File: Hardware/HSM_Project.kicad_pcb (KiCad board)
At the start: 2 copper layers, 139 x 101.5 mm, 116 parts, among them J1 Conn_01x02_Pin, J10 VL530X Connector, J11 VL530X Connector, J12 VL530X Connector, J13 VL530X Connector, J14 Conn_01x04_Pin, J15 BNO055 Breakout, J16 HC-05 Breakout Board, J17 Conn_01x04_Pin, J18 Conn_01x02_Pin, J19 Conn_01x02_Pin, J2 MP1584 Breakout, J20 Conn_01x04_Pin, J3 DRV8833 Breakout, J4 TEENSY_4.1, J8 VL530X Connector, J9 VL530X Connector, Q1 Q_NMOS_GSD, Q10 Q_NMOS_GSD, Q11 Q_NMOS_GSD, Q12 Q_NMOS_GSD, Q13 TEFT4300, Q2 Q_NMOS_GSD, Q3 TEFT4300, Q4 TEFT4300, Q5 TEFT4300, Q6 TEFT4300, Q7 TEFT4300, Q8 Q_NMOS_GSD, Q9 Q_NMOS_GSD, SW1 SW_SPDT, SW2 SW_SPDT, SW3 SW_Push, SW4 SW_Push

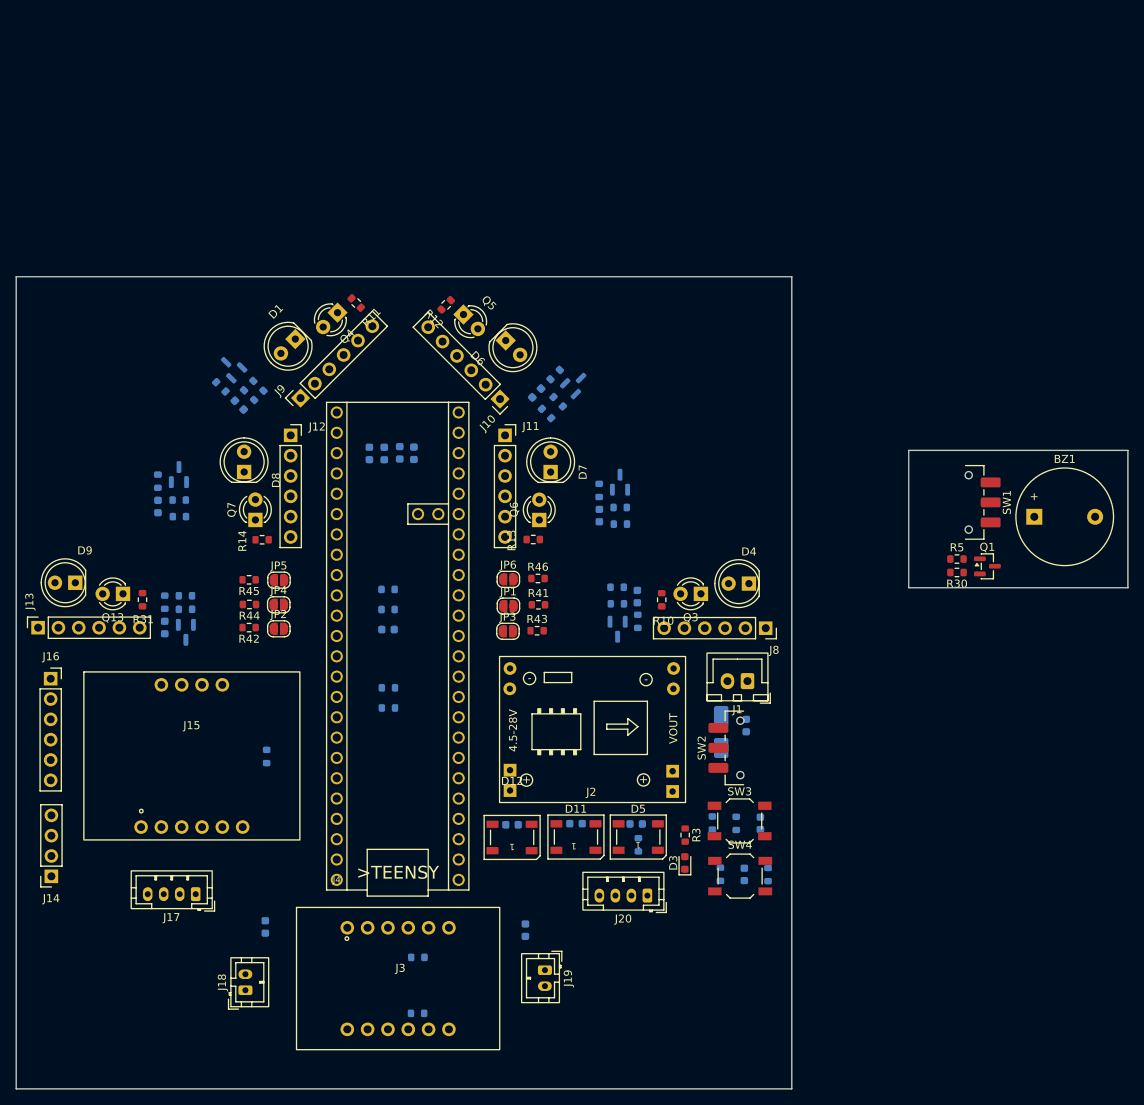
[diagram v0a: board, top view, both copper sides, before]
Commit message: Added the mounting holes, kill iwtch for the moto,removed resistors from xshut, and some others
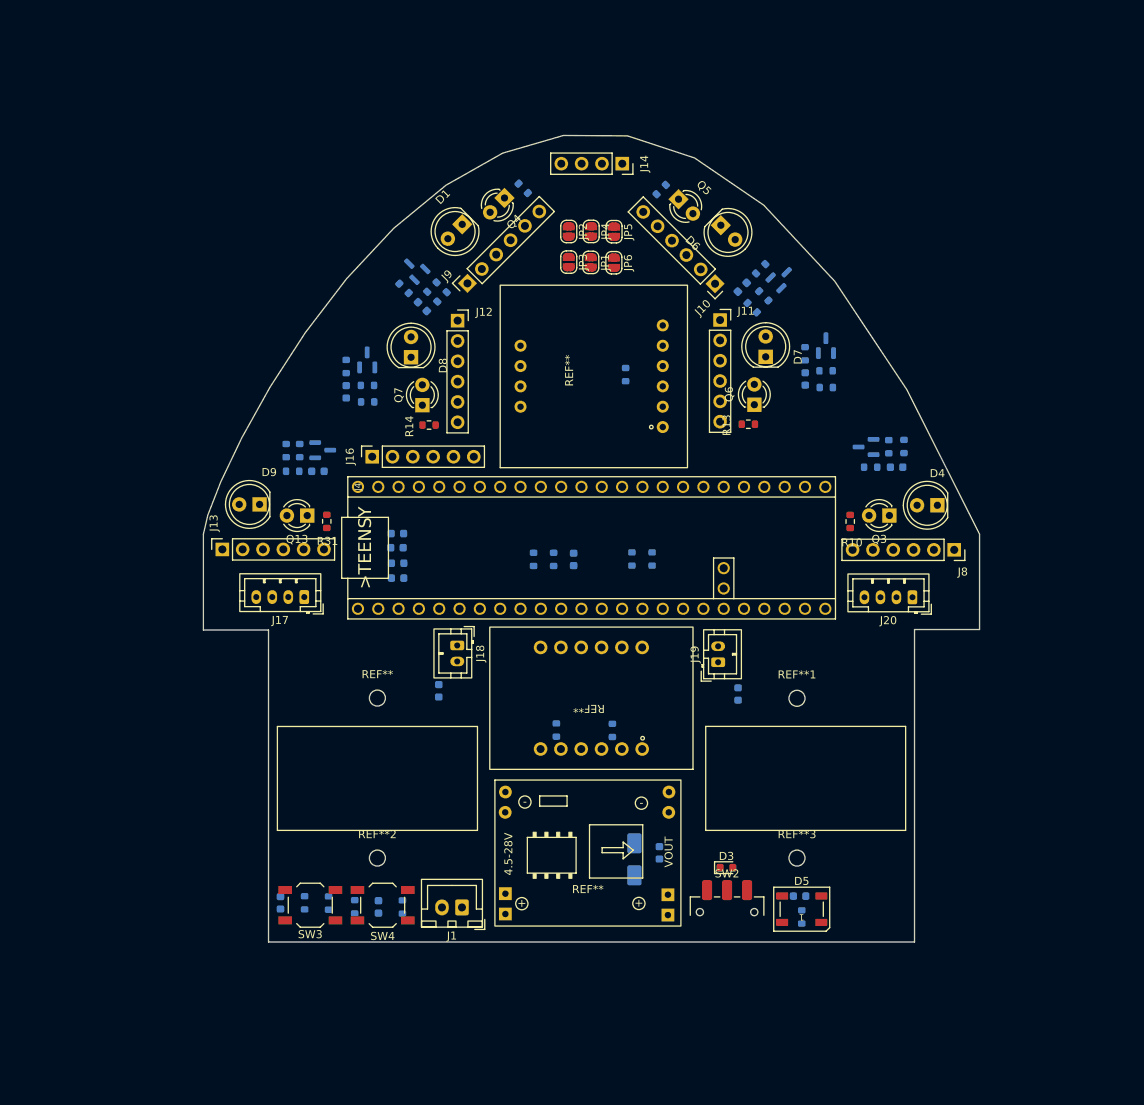
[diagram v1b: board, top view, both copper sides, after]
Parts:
- removed BZ1: Buzzer, Buzzer_Beeper:Buzzer_12x9.5RM7.6
- removed C14, C15: 100n, Capacitor_SMD:C_0603_1608Metric
- removed D11, D12: WS2812B, LED_SMD:LED_WS2812B_PLCC4_5.0x5.0mm_P3.2mm
- removed J15: BNO055 Breakout, Micromouse_Footprints:BNO055
- removed J2: MP1584 Breakout, Micromouse_Footprints:SRT_MPT1584EN_Module
- removed J3: DRV8833 Breakout, Micromouse_Footprints:DRV8833
- removed Q1: Q_NMOS_GSD, Package_TO_SOT_SMD:SOT-23
- removed R30, R41, R42, R43, R44, R45, R46, R5: 10k, Resistor_SMD:R_0603_1608Metric
- removed SW1: SW_SPDT, Button_Switch_SMD:SW_SPDT_CK_JS102011SAQN
- added REF**: MP1584, Micromouse_Footprints:MP1584, F.Cu at (153.0, 120.9)
- added REF**: MountingHole_2mm, MountingHole:MountingHole_2mm, F.Cu at (126.8, 100.5)
- added REF**: BNO055, Micromouse_Footprints:BNO055, F.Cu at (154.0, 60.0)
- added REF**: DRV8833, Micromouse_Footprints:DRV8833, F.Cu at (153.5, 100.5)
- added REF**1: MountingHole_2mm, MountingHole:MountingHole_2mm, F.Cu at (179.2, 100.5)
- added REF**2: MountingHole_2mm, MountingHole:MountingHole_2mm, F.Cu at (126.8, 120.5)
- added REF**3: MountingHole_2mm, MountingHole:MountingHole_2mm, F.Cu at (179.2, 120.5)
- R11, R12, R3: moved to B.Cu
- moved J14 114.1 mm to (157.4, 33.7), turned to -90 degrees
- moved R47 65.5 mm to (157.8, 60.1)
- moved JP2 61.5 mm to (150.7, 42.2), turned to -90 degrees
- moved JP4 60.9 mm to (153.5, 42.2), turned to -90 degrees
- moved C17 60.8 mm to (114.7, 126.1), turned to -90 degrees
- moved JP5 60.4 mm to (156.3, 42.2), turned to -90 degrees
- moved R27 54.9 mm to (117.7, 126.1), turned to -90 degrees
- moved SW3 54.7 mm to (118.4, 126.4), turned to 0 degrees
- moved R1 51.8 mm to (123.9, 126.6), turned to -90 degrees
- moved J18 50.6 mm to (136.8, 93.9), turned to -90 degrees
- moved J20 49.9 mm to (193.7, 87.9)
- moved J4 49.2 mm to (124.3, 74.1), turned to -90 degrees
- moved R2 49.0 mm to (120.7, 126.1), turned to -90 degrees
- moved J16 48.8 mm to (126.1, 70.3), turned to 90 degrees
- moved JP3 46.8 mm to (150.7, 46.0), turned to -90 degrees
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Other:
- board size 139 x 101.5 mm -> 97 x 100.8 mm
- board text added: "${REFERENCE}"

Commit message: 1)PCB tracing continued, power traces need to verified,signal traces almost done except xshut, need to verify drv8833 dimesnions, should resolve teensy 4.1 error, switches footprint need to be changed. 2) changed schematic for optimum tracing in pcb editor,removed oled and added one more extra i2c bus to prevent i2c locking
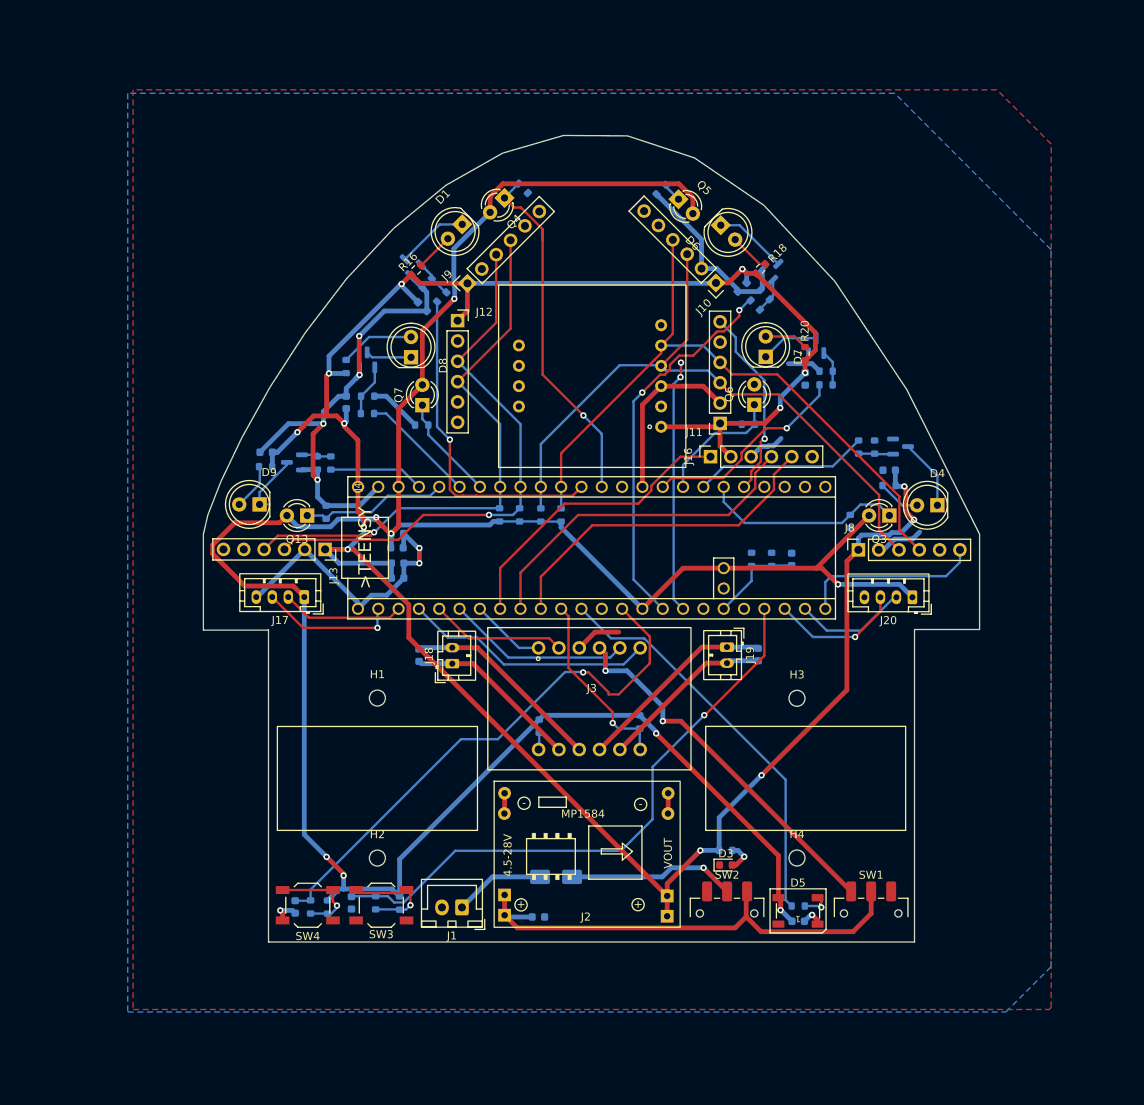
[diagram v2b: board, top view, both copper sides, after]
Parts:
- removed J14: Conn_01x04_Pin, Connector_PinSocket_2.54mm:PinSocket_1x04_P2.54mm_Vertical
- removed JP1, JP2, JP3, JP4, JP5, JP6: SolderJumper_2_Bridged, Jumper:SolderJumper-2_P1.3mm_Open_RoundedPad1.0x1.5mm
- removed R47: 10k, Resistor_SMD:R_0603_1608Metric
- removed REF**: MP1584, Micromouse_Footprints:MP1584
- removed REF**, REF**1, REF**2, REF**3: MountingHole_2mm, MountingHole:MountingHole_2mm
- removed REF**: BNO055, Micromouse_Footprints:BNO055
- removed REF**: DRV8833, Micromouse_Footprints:DRV8833
- added H1: MountingHole, MountingHole:MountingHole_2mm, F.Cu at (126.8, 100.5)
- added H2: MountingHole, MountingHole:MountingHole_2mm, F.Cu at (126.8, 120.5)
- added H3: MountingHole, MountingHole:MountingHole_2mm, F.Cu at (179.2, 100.5)
- added H4: MountingHole, MountingHole:MountingHole_2mm, F.Cu at (179.2, 120.5)
- added J2: MP1584 Breakout, Micromouse_Footprints:SRT_MPT1584EN_Module, F.Cu at (152.1, 123.2)
- added J3: DRV8833 Breakout, Micromouse_Footprints:DRV8833, F.Cu at (153.3, 100.6)
- added J5: BNO055 Breakout, Micromouse_Footprints:BNO055, F.Cu at (153.8, 60.0)
- added R30: 4.7k, Resistor_SMD:R_0603_1608Metric, B.Cu at (149.7, 77.6)
- added R5: 4.7k, Resistor_SMD:R_0603_1608Metric, B.Cu at (147.2, 77.6)
- added SW1: SW_SPDT, Button_Switch_SMD:SW_SPDT_CK_JS102011SAQN, F.Cu at (188.5, 127.4)
- R10, R13, R14, R31: moved to B.Cu
- R16, R18, R20: moved to F.Cu
- moved J16 42.3 mm to (168.4, 70.3)
- moved C8 27.2 mm to (178.6, 83.2)
- moved R6 27.2 mm to (173.5, 83.2)
- moved R7 27.2 mm to (176.1, 83.2)
- moved R24 19.8 mm to (142.0, 77.6), turned to 90 degrees
- moved C10 17.1 mm to (146.9, 127.9), turned to 0 degrees
- moved R23 15.1 mm to (144.6, 77.6), turned to 90 degrees
- moved J11 12.9 mm to (169.6, 66.2), turned to 180 degrees
- moved J13 12.8 mm to (120.2, 81.9), turned to -90 degrees
- moved J8 12.0 mm to (186.9, 82.0), turned to 90 degrees
- moved C16 10.4 mm to (116.5, 126.6)
- moved D2 10.0 mm to (149.1, 122.8), turned to 180 degrees
- moved R33 9.36 mm to (120.5, 126.6)
- moved SW4 9.36 mm to (118.1, 126.4)
- moved R2 8.88 mm to (129.5, 126.1)
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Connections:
- net /Control Unit/STATUS renamed /Control Unit/BATTERY_LED
- D5 pad 2: Net-(D11-DIN) -> unconnected-(D5-DOUT-Pad2)
- J10 pad 3: /Control Unit/SDA0 -> /Control Unit/SDA1
- J10 pad 4: /Control Unit/SCL0 -> /Control Unit/SCL1
- J11 pad 3: /Control Unit/SDA0 -> /Control Unit/SDA1
- J11 pad 4: /Control Unit/SCL0 -> /Control Unit/SCL1
- J4 pad D11: /Control Unit/BUZZER -> unconnected-(J4-(SDO)D11-PadD11)
- J4 pad D14: /Control Unit/SENS_FRONT -> /Control Unit/SENS_FRONT_LEFT
- J4 pad D15: /Control Unit/SENS_FRONT_LEFT -> /Control Unit/EMITTER_FRONT_LEFT
- J4 pad D16: /Control Unit/SENS_FRONT_RIGHT -> /Control Unit/SCL1
- J4 pad D17: /Control Unit/SENS_RIGHT -> /Control Unit/SDA1
- J4 pad D20: /Control Unit/EMITTER_FRONT -> /Control Unit/SENS_LEFT
- J4 pad D21: /Control Unit/EMITTER_FRONT_LEFT -> /Control Unit/EMITTER_LEFT
- J4 pad D22: /Control Unit/EMITTER_FRONT_RIGHT -> /Control Unit/SENSE_FRONT_2
- J4 pad D23: /Control Unit/EMITTER_RIGHT -> /Control Unit/EMIITER_FRONT_2
- J4 pad D24: /Control Unit/SENS_LEFT -> /Control Unit/EMITTER_FRONT_RIGHT
- J4 pad D25: /Control Unit/EMITTER_LEFT -> /Control Unit/SENS_FRONT_RIGHT
- J4 pad D38: unconnected-(J4-A14-PadD38) -> /Control Unit/SENS_FRONT
- J4 pad D39: /Control Unit/IMU_INT -> /Control Unit/EMITTER_FRONT
- J4 pad D40: /Control Unit/SENSE_FRONT_2 -> /Control Unit/SENS_RIGHT
- J4 pad D41: /Control Unit/EMIITER_FRONT_2 -> /Control Unit/EMITTER_RIGHT
- J8 pad 3: /Control Unit/SDA0 -> /Control Unit/SDA1
- J8 pad 4: /Control Unit/SCL0 -> /Control Unit/SCL1
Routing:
- net +3.3V: track 0.00 -> 328.4 mm, vias 0 -> 8
- net /Control Unit/VOUT: track 0.00 -> 302.9 mm, vias 0 -> 13
- net GND: track 0.00 -> 182.3 mm, vias 0 -> 8
- net /Control Unit/SCL1: track 0.00 -> 84.7 mm
- net /Control Unit/SDA1: track 0.00 -> 84.3 mm
- net /Control Unit/ALGO_CONTROL: track 0.00 -> 74.4 mm, vias 0 -> 1
- net /Control Unit/SCL0: track 0.00 -> 70.1 mm, vias 0 -> 1
- net /Control Unit/SDA0: track 0.00 -> 68.5 mm, vias 0 -> 1
- net /Control Unit/RUN_MODE_GPIO: track 0.00 -> 68.1 mm, vias 0 -> 1
- net IN+: track 0.00 -> 60.8 mm
- net /Control Unit/BATTERY_LED: track 0.00 -> 50.5 mm
- net /Control Unit/EMITTER_FRONT_RIGHT: track 0.00 -> 48.2 mm, vias 0 -> 2
- net Net-(J3-VCC): track 0.00 -> 46.4 mm, vias 0 -> 2
- net /Control Unit/SENS_FRONT_LEFT: track 0.00 -> 45.5 mm, vias 0 -> 1
- net /Control Unit/BT_RX: track 0.00 -> 43.0 mm
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- added copper zone on B.Cu, net GND
- added copper zone on F.Cu, net GND
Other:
- board text removed: "${REFERENCE}"

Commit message: PCB tracing, rectified most of the errors and warnings in drc,updated the drv8833 footprint  and have to replace it will old footprint in the pcb, need to rectify the little left over error[4] and warnings[10](related to footprint copy)
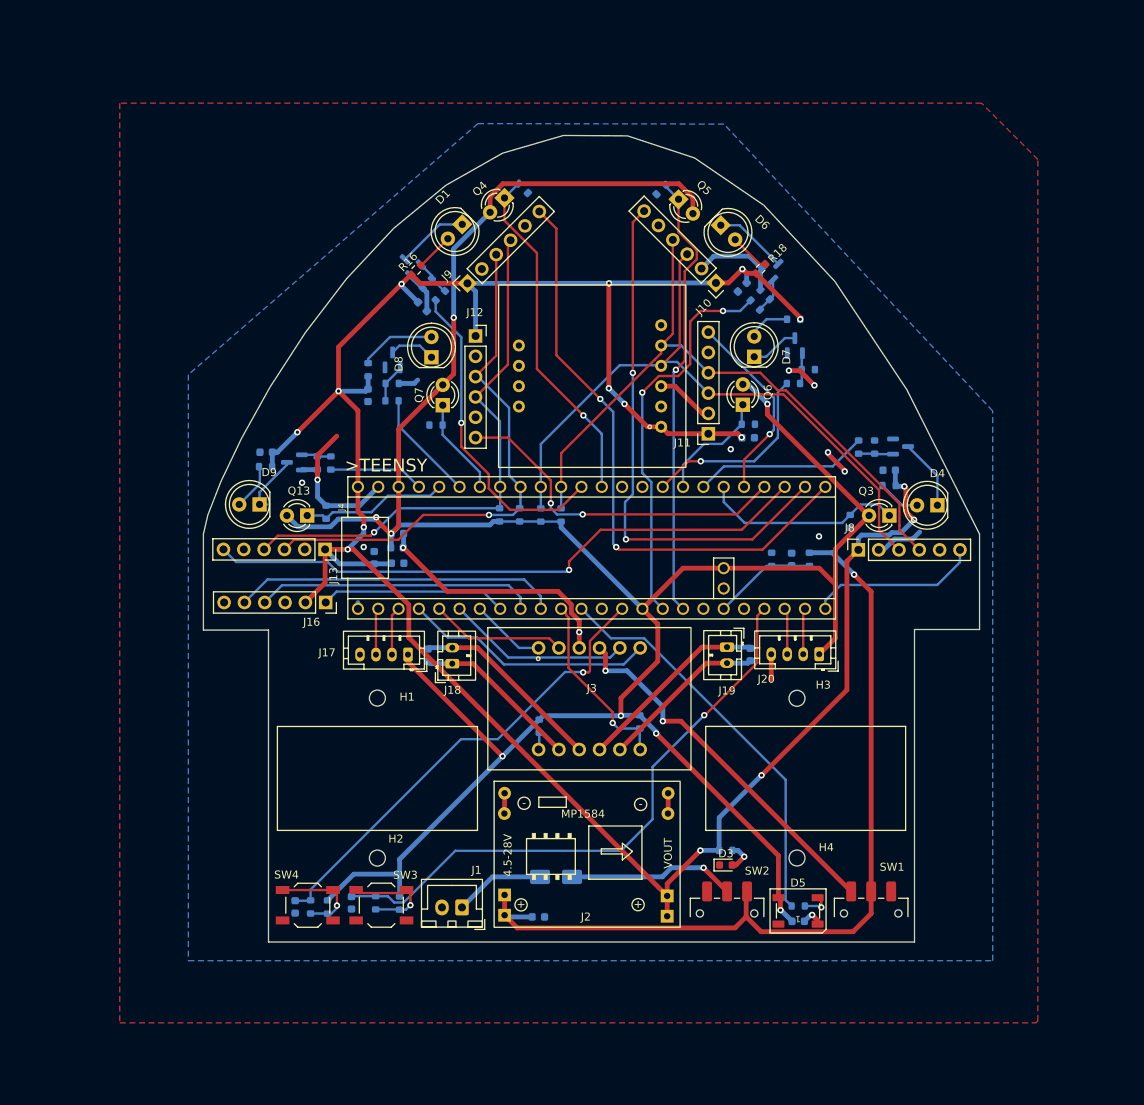
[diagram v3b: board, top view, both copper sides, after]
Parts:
- R20: moved to B.Cu
- moved J16 51.4 mm to (120.3, 88.5), turned to -90 degrees
- moved J17 14.8 mm to (130.6, 95.1)
- moved J20 13.7 mm to (182.0, 95.0)
- moved C11 10.2 mm to (173.1, 68.0), turned to 0 degrees
- moved R6 7.23 mm to (180.8, 83.2)
- moved R20 4.54 mm to (178.8, 53.1), turned to 180 degrees
- moved R19 4.08 mm to (178.8, 61.2)
- moved C4 3.88 mm to (126.4, 83.0), turned to 90 degrees
- moved R21 3.45 mm to (128.6, 63.3)
- moved R37 3.45 mm to (128.6, 61.2)
- moved Q11 3.18 mm to (128.7, 58.2)
- moved J12 2.95 mm to (139.0, 55.2)
- moved C12 2.87 mm to (125.6, 62.7), turned to -90 degrees
- moved R22 2.78 mm to (125.6, 59.5)
- moved Q10 2.67 mm to (178.9, 56.4)
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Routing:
- net GND: track 182.3 -> 105.4 mm, vias 8 -> 12
- net /Control Unit/XSHUT_TOF4: track 0.00 -> 76.3 mm, vias 0 -> 1
- net /Control Unit/XSHUT_TOF2: track 0.00 -> 75.4 mm, vias 0 -> 2
- net /Control Unit/XSHUT_TOF3: track 0.00 -> 67.3 mm, vias 0 -> 2
- net IN+: track 60.8 -> 108.0 mm, vias 0 -> 1
- net /Control Unit/XSHUT_TOF5: track 0.00 -> 43.5 mm, vias 0 -> 2
- net /Control Unit/SENS_FRONT_RIGHT: track 34.1 -> 56.3 mm, vias 2 -> 1
- net /Control Unit/AT_COMMAND_LINE: track 37.5 -> 23.3 mm
- net /Control Unit/ENC1_A: track 17.2 -> 5.84 mm, vias 1 -> 0
- net /Control Unit/ENC2_A: track 16.5 -> 5.81 mm, vias 1 -> 0
- net /Control Unit/ENC1_B: track 15.3 -> 6.06 mm
- net /Control Unit/RUN_MODE_GPIO: track 68.1 -> 59.0 mm
- net /Control Unit/ENC2_B: track 14.3 -> 5.77 mm
- net /Control Unit/BT_RX: track 43.0 -> 34.9 mm
- net /Control Unit/VOUT: track 302.9 -> 310.2 mm, vias 13 -> 15
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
